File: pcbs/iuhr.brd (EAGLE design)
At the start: 38.4 x 23 mm, 78 parts, among them Q1 20.000MHz

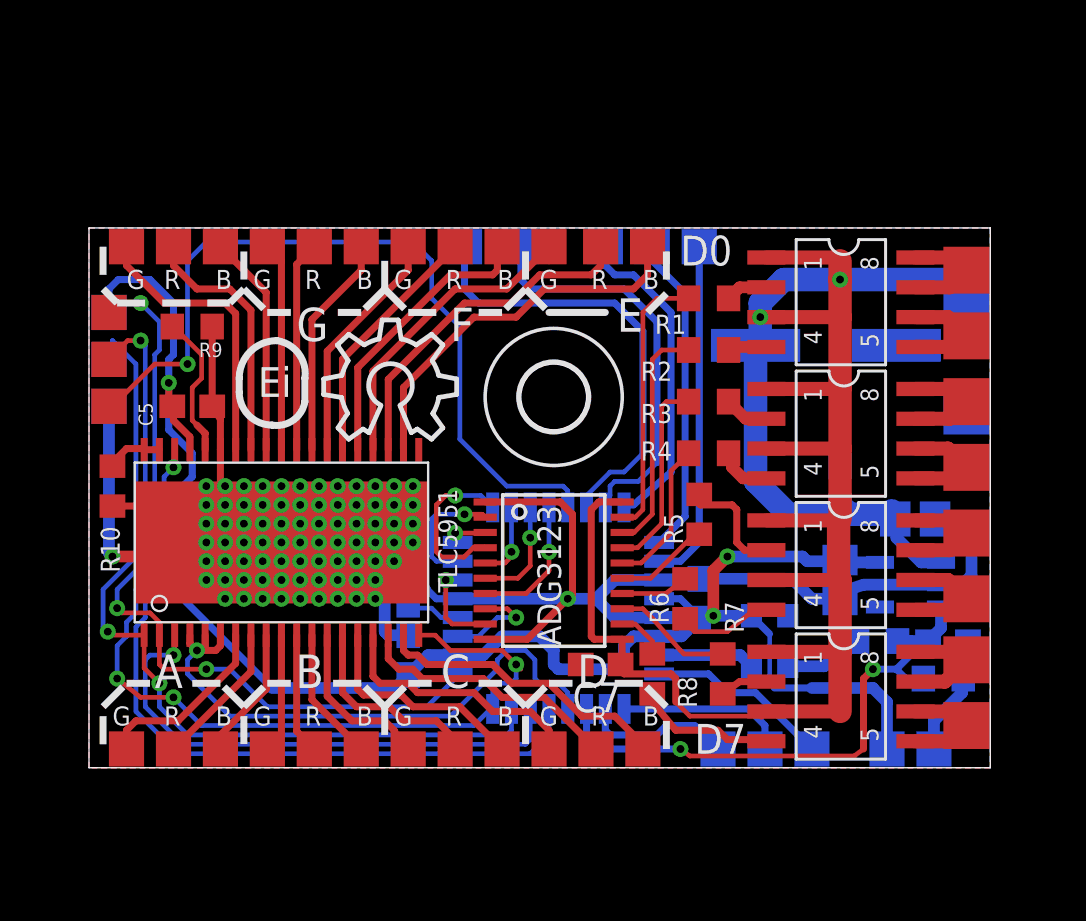
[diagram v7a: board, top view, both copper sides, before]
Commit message: Add p-channel mosfet to be able to shut off 12V part.
TODO: find space on board
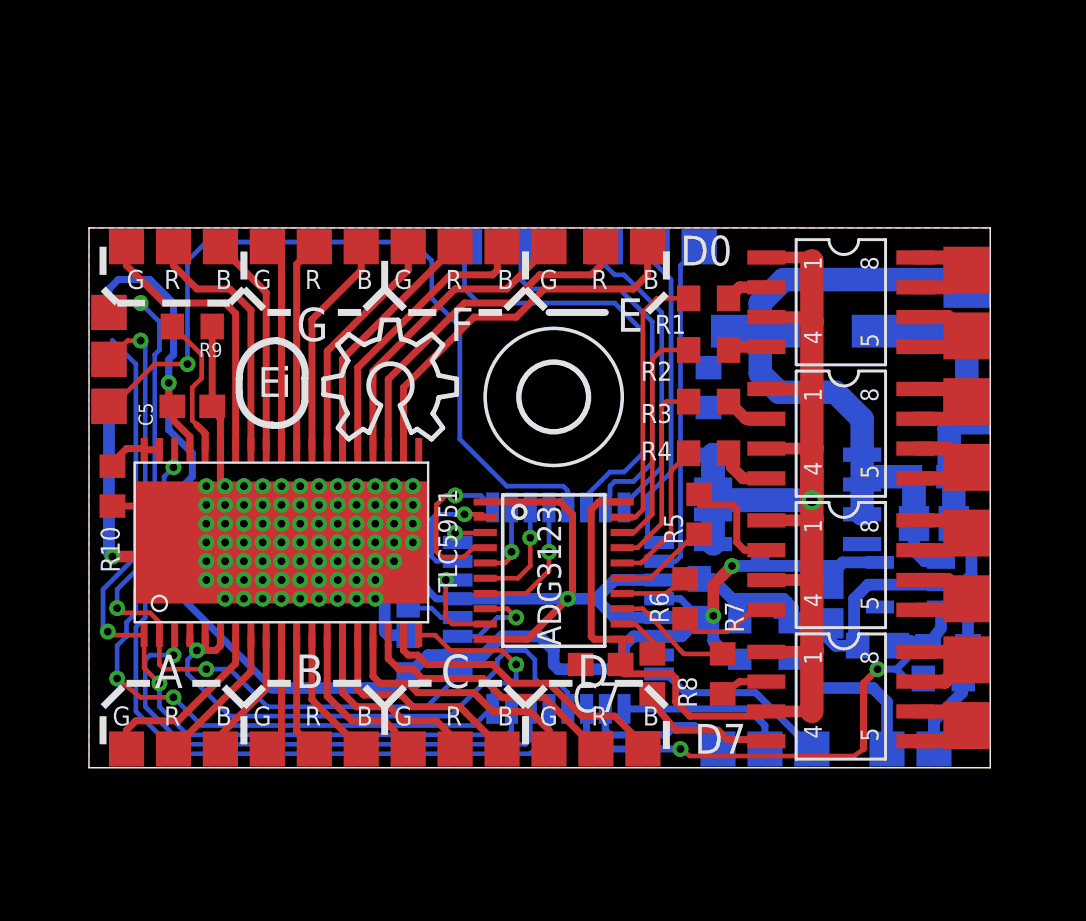
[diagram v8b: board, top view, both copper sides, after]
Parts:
- added Q2: MOSFET-NCHANNELSMD, SparkFun:SOT23-3
- added R13: 10k, resistor:R0603
- added U$2: IRF7416, ShortCircuitRobotics:SO8-2
- moved C11 3.82 mm to (35.8, 12.4), turned to 180 degrees
- moved C6 1.17 mm to (31.4, 7.00)
- moved C4 0.82 mm to (36.0, 10.4)
- moved 12V_IN 0.60 mm to (37.4, 20.6)
- moved C13 0.60 mm to (31.4, 18.6)
- moved C8 0.20 mm to (36.6, 5.20)
- moved R11 0.20 mm to (33.6, 5.20)
- moved Q1 0.20 mm to (28.8, 5.40), turned to 180 degrees
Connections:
- new net N$61: Q2.3, R13.1, U$2.4
- new net VPP: ADG3123.11, ADG3123.20, C7.1, IRF7104.1, IRF7104.3, U$2.5, U$2.6, U$2.7, U$2.8, U$3.1, U$3.3, U$4.1, U$4.3, U$6.1, U$6.3
- net +12V: now also R13.2, U$2.1, U$2.2, U$2.3; no longer ADG3123.11, ADG3123.20, C7.1, IRF7104.1, IRF7104.3, U$3.1, U$3.3, U$4.1, U$4.3, U$6.1, U$6.3
- net GND: now also Q2.2
- net ON: now also Q2.1
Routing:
- net VPP: track 0.00 -> 62.2 mm, vias 0 -> 1
- net +12V: track 90.3 -> 29.9 mm, vias 2 -> 0
- net GND: track 91.8 -> 103.9 mm
- net CLK_STM: track 4.13 -> 0.00 mm
- net VCC: track 72.6 -> 69.6 mm
- net N$21: track 13.8 -> 13.0 mm
- removed copper zone on layer 16, net GND
